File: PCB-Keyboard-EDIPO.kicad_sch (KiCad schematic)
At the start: 0 parts

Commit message: MCU Edits
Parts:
- added C1: 1u, symbol Device:C_Small
- added C2, C3: 22p, symbol Device:C_Small
- added C4, C5, C6, C7: 0.1u, symbol Device:C_Small
- added C8: 10u, symbol Device:C_Small
- added J1: AVR-ISP-6, symbol Connector:AVR-ISP-6
- added R1: 10k, symbol Device:R_Small
- added U1: ATmega32U4-A, Package_QFP:TQFP-44_10x10mm_P0.8mm, symbol MCU_Microchip_ATmega:ATmega32U4-A
- added Y1: XTAL, symbol Device:Crystal_GND24_Small
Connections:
- new net: R1.1, U1.33 (~{HWB}/PE2)
- new net: C1.1, U1.6 (UCAP)
- new net +5V: C4.1, C5.1, C6.1, C7.1, C8.1, J1.2 (VCC), U1.14 (VCC), U1.2 (UVCC), U1.24 (AVCC), U1.34 (VCC), U1.44 (AVCC)
- new net D+: U1.4 (D+)
- new net D-: U1.3 (D-)
- new net GND: C1.2, C2.2, C3.2, C4.2, C5.2, C6.2, C7.2, C8.2, J1.6 (GND), R1.2, U1.15 (GND), U1.23 (GND), U1.35 (GND), U1.43 (GND), U1.5 (UGND), Y1.2, Y1.4
- new net MISO: J1.1 (MISO), U1.11 (PB3)
- new net MOSI: J1.4 (MOSI), U1.10 (PB2)
- new net RESET: U1.13 (~{RESET})
- new net RST: J1.5 (~{RST})
- new net SCK: J1.3 (SCK), U1.9 (PB1)
- new net XTAL1: C3.1, U1.17 (XTAL1), Y1.1
- new net XTAL2: C2.1, U1.16 (XTAL2), Y1.3
- no-connect marks 0 -> 2

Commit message: Part 1
MCU, USB Port, Switch Matrix
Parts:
- added F1: 500m, symbol Device:Polyfuse_Small
- added R2: 10k, symbol Device:R_Small
- added R3, R4: 22, symbol Device:R_Small
- added R5, R6: 5.1k, symbol Device:R_Small
- added SW1: SW_Push_Reset, symbol local:SW_SKQG
- added U2: PRTR5V0U2X, symbol random-keyboard-parts:PRTR5V0U2X
- added USB1: HRO-TYPE-C-31-M-12, symbol Type-C:HRO-TYPE-C-31-M-12
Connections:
- net RST is gone; now on net RESET: J1.5 (~{RST})
- net +5V: now also U1.7 (VBUS), F1.2, R2.2
- net D+: now also R4.2
- net D-: now also R3.2
- net GND: now also R5.1, R6.1, SW1.2, U2.1 (GND), USB1.1 (GND), USB1.12 (GND), USB1.13 (SHIELD)
- new net: R5.2, USB1.10 (CC2)
- new net: R6.2, USB1.4 (CC1)
- new net DN: R3.1, U2.3 (IO2), USB1.5 (DN2), USB1.7 (DN1)
- new net DP: R4.1, U2.2 (IO1), USB1.6 (DP1), USB1.8 (DP2)
- new net Reset: R2.1, SW1.1
- new net VCC: F1.1, U2.4 (VCC), USB1.11 (VBUS), USB1.2 (VBUS)
- no-connect marks 2 -> 6
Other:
- moved on the sheet: C2, C3, J1, Y1

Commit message: Matrix Strart
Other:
- added sheet matrix (matrix.kicad_sch)
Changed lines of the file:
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@@
+		)
+	)
+	(sheet
+		(at 88.9 38.1)
+		(size 25.4 12.7)
+		(exclude_from_sim no)
+		(in_bom yes)
+		(on_board yes)
+		(dnp no)
+		(fields_autoplaced yes)
+		(stroke
+			(width 0.1524)
+			(type solid)
+		)
+		(fill
+			(color 0 0 0 0.0000)
+		)
+		(property "Sheetname" "matrix"
+			(at 88.9 37.3884 0)
+			(effects
+				(font
+					(size 1.27 1.27)
+				)
+				(justify left bottom)
+			)
+		)
+		(property "Sheetfile" "matrix.kicad_sch"
+			(at 88.9 51.3846 0)
+			(effects
+				(font
+					(size 1.27 1.27)
+				)
+				(justify left top)
+			)
+		)
+		(instances
+			(project "PCB-Keyboard-EDIPO"
+				(path "/8d1b740c-cc3b-4519-96ee-3a49fcc08051"
+					(page "2")
+				)
+			)
 		)
 	)

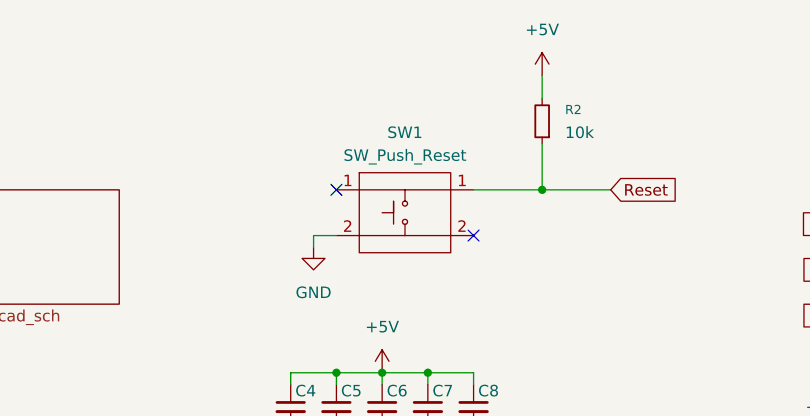
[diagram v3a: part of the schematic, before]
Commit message: Matrix Design and slight keycap config
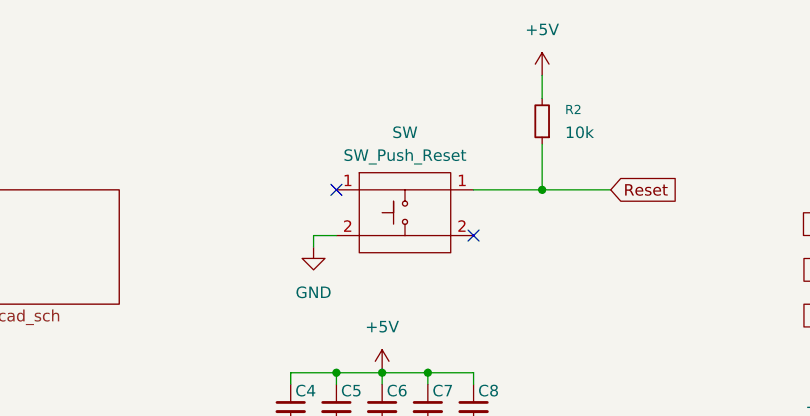
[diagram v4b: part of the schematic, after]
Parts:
- renumbered SW1 to SW
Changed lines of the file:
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@@
 		(dnp no)
 		(fields_autoplaced yes)
-		(property "Reference" "SW1"
+		(property "Reference" "SW"
 			(at 146.05 31.75 0)
 			(effects
@@
 			(project ""
 				(path "/8d1b740c-cc3b-4519-96ee-3a49fcc08051"
-					(reference "SW1")
+					(reference "SW")
 					(unit 1)
 				)

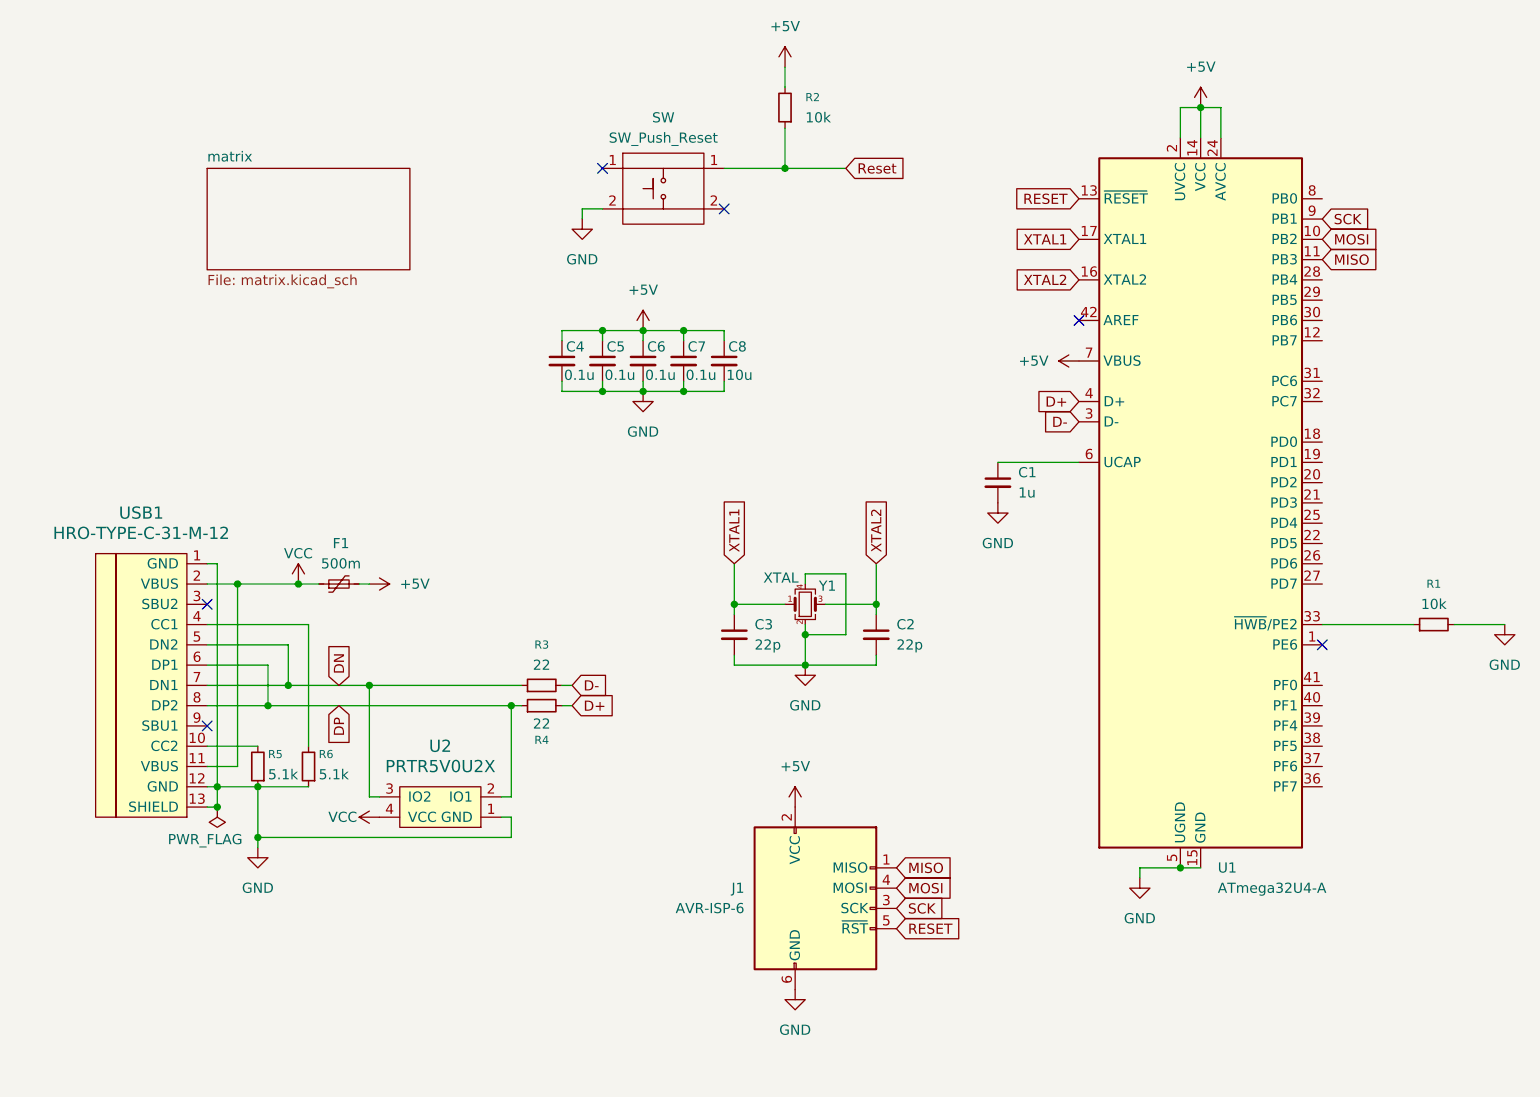
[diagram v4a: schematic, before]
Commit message: Matrix Design Done
still need to assign footprints
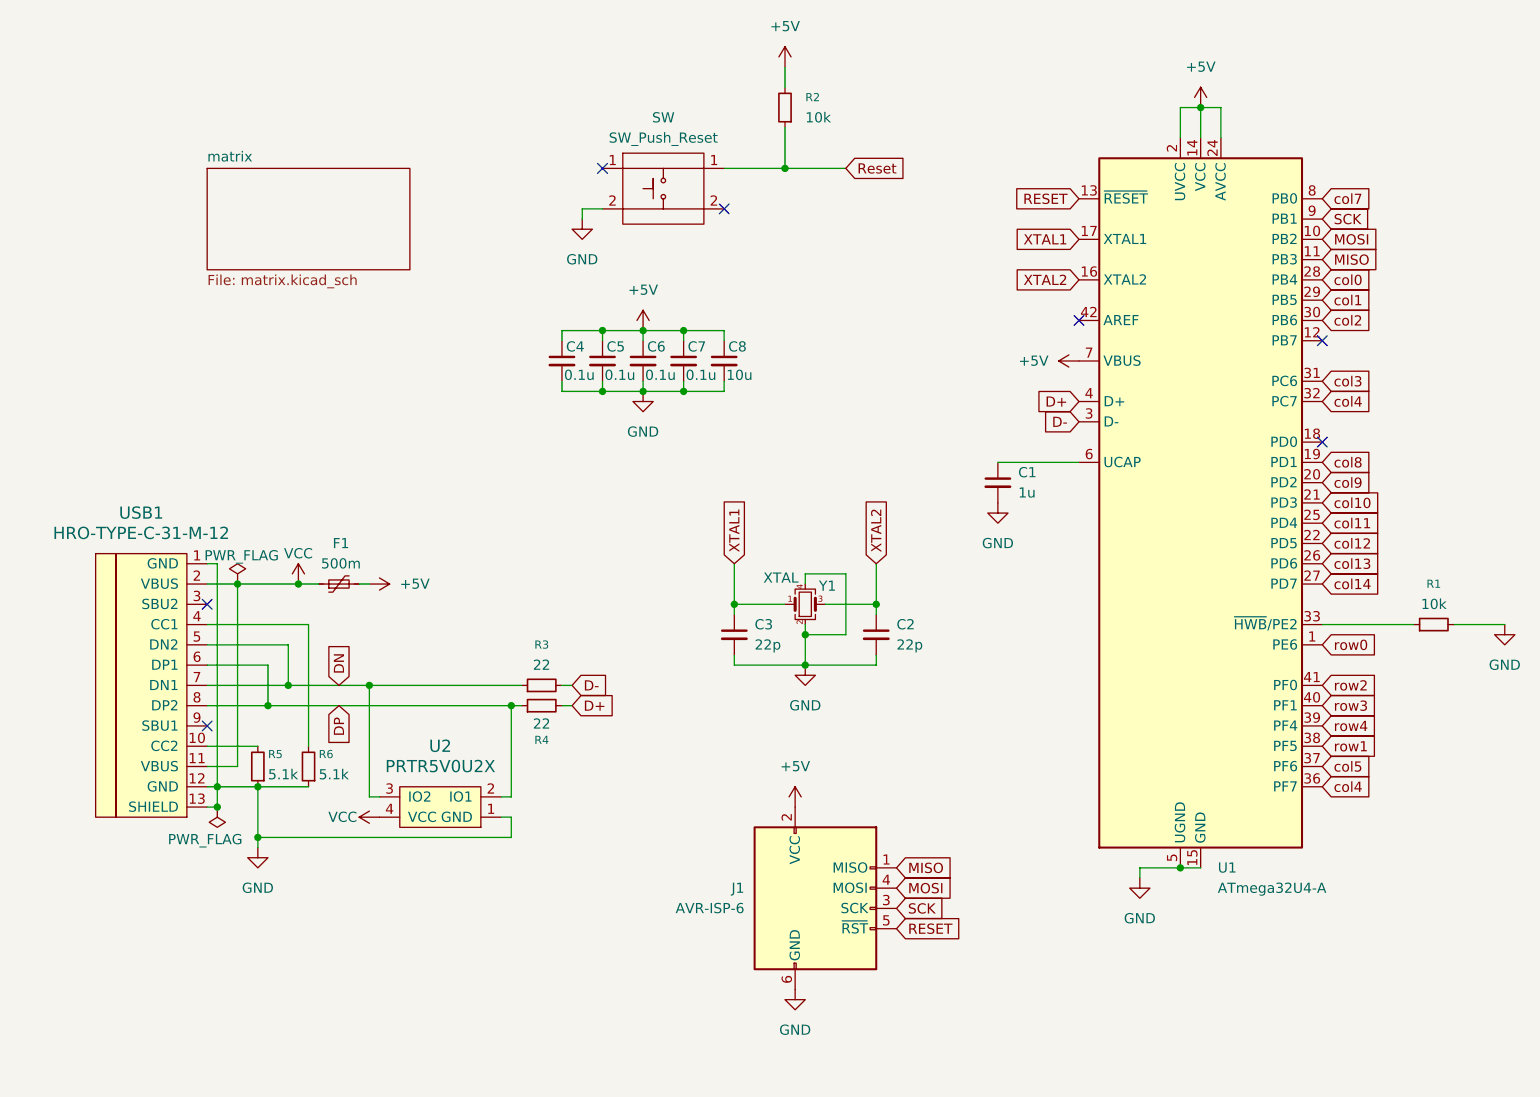
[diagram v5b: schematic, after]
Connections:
- net row0: now reaches U1.1 (PE6)
- net col8: now reaches U1.19 (PD1)
- net col9: now reaches U1.20 (PD2)
- net col10: now reaches U1.21 (PD3)
- net col12: now reaches U1.22 (PD5)
- net col11: now reaches U1.25 (PD4)
- net col13: now reaches U1.26 (PD6)
- net col14: now reaches U1.27 (PD7)
- net col0: now reaches U1.28 (PB4)
- net col1: now reaches U1.29 (PB5)
- net col2: now reaches U1.30 (PB6)
- net col3: now reaches U1.31 (PC6)
- net col4: now reaches U1.32 (PC7)
- net col4: now also U1.36 (PF7)
- net col5: now reaches U1.37 (PF6)
- net row1: now reaches U1.38 (PF5)
- net row4: now reaches U1.39 (PF4)
- net row3: now reaches U1.40 (PF1)
- net row2: now reaches U1.41 (PF0)
- net col7: now reaches U1.8 (PB0)
- no-connect marks 6 -> 7

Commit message: Footprints Added
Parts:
- C1, C2, C3, C4, C5, C6, C7, C8: footprint (none) -> Capacitor_SMD:C_0805_2012Metric_Pad1.18x1.45mm_HandSolder
- F1: footprint (none) -> Fuse:Fuse_1206_3216Metric_Pad1.42x1.75mm_HandSolder
- J1: footprint (none) -> random-keyboard-parts:Reset_Pretty-Mask
- R1, R2, R3, R4, R5, R6: footprint (none) -> Resistor_SMD:R_0805_2012Metric_Pad1.20x1.40mm_HandSolder
- SW68: renamed from SW; footprint (none) -> Button_Switch_SMD:SW_SPST_SKQG_WithStem
- U2: footprint (none) -> random-keyboard-parts:SOT143B
- USB1: footprint (none) -> Type-C:HRO-TYPE-C-31-M-12-HandSoldering
- Y1: footprint (none) -> Crystal:Crystal_SMD_3225-4Pin_3.2x2.5mm_HandSoldering
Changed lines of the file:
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@@
 			)
 		)
-		(property "Footprint" ""
+		(property "Footprint" "Capacitor_SMD:C_0805_2012Metric_Pad1.18x1.45mm_HandSolder"
 			(at 138.43 62.23 0)
 			(effects
@@
 			)
 		)
-		(property "Footprint" ""
+		(property "Footprint" "Capacitor_SMD:C_0805_2012Metric_Pad1.18x1.45mm_HandSolder"
 			(at 154.94 96.52 0)
 			(effects
@@
 			)
 		)
-		(property "Footprint" ""
+		(property "Footprint" "Resistor_SMD:R_0805_2012Metric_Pad1.20x1.40mm_HandSolder"
 			(at 130.81 102.87 0)
 			(effects
@@
 			)
 		)
-		(property "Footprint" ""
+		(property "Footprint" "Fuse:Fuse_1206_3216Metric_Pad1.42x1.75mm_HandSolder"
 			(at 110.49 88.9 0)
 			(effects
@@
 			)
 		)
-		(property "Footprint" ""
+		(property "Footprint" "Capacitor_SMD:C_0805_2012Metric_Pad1.18x1.45mm_HandSolder"
 			(at 172.72 96.52 0)
 			(effects
@@
 			)
 		)
-		(property "Footprint" ""
+		(property "Footprint" "Resistor_SMD:R_0805_2012Metric_Pad1.20x1.40mm_HandSolder"
 			(at 95.25 113.03 0)
 			(effects
@@
 			)
 		)
-		(property "Footprint" ""
+		(property "Footprint" "Resistor_SMD:R_0805_2012Metric_Pad1.20x1.40mm_HandSolder"
 			(at 161.29 30.48 0)
 			(effects
@@
 			)
 		)
-		(property "Footprint" ""
+		(property "Footprint" "random-keyboard-parts:Reset_Pretty-Mask"
 			(at 158.75 129.54 90)
 			(effects
@@
 			)
 		)
-		(property "Footprint" ""
+		(property "Footprint" "random-keyboard-parts:SOT143B"
 			(at 118.11 118.11 0)
 			(effects
@@
 			)
 		)
-		(property "Footprint" ""
+		(property "Footprint" "Capacitor_SMD:C_0805_2012Metric_Pad1.18x1.45mm_HandSolder"
 			(at 143.51 62.23 0)
 			(effects
@@
 			)
 		)
-		(property "Footprint" ""
+		(property "Footprint" "Type-C:HRO-TYPE-C-31-M-12-HandSoldering"
 			(at 86.36 101.6 0)
 			(effects
@@
 			)
 		)
-		(property "Footprint" ""
+		(property "Footprint" "Resistor_SMD:R_0805_2012Metric_Pad1.20x1.40mm_HandSolder"
 			(at 130.81 105.41 0)
 			(effects
@@
 			)
 		)
-		(property "Footprint" ""
+		(property "Footprint" "Resistor_SMD:R_0805_2012Metric_Pad1.20x1.40mm_HandSolder"
 			(at 101.6 113.03 0)
 			(effects
@@
 			)
 		)
-		(property "Footprint" ""
+		(property "Footprint" "Capacitor_SMD:C_0805_2012Metric_Pad1.18x1.45mm_HandSolder"
 			(at 148.59 62.23 0)
 			(effects
@@
 			)
 		)
-		(property "Footprint" ""
+		(property "Footprint" "Capacitor_SMD:C_0805_2012Metric_Pad1.18x1.45mm_HandSolder"
 			(at 153.67 62.23 0)
 			(effects
@@
 			)
 		)
-		(property "Footprint" ""
+		(property "Footprint" "Capacitor_SMD:C_0805_2012Metric_Pad1.18x1.45mm_HandSolder"
 			(at 187.96 77.47 0)
 			(effects
@@
 			)
 		)
-		(property "Footprint" ""
+		(property "Footprint" "Crystal:Crystal_SMD_3225-4Pin_3.2x2.5mm_HandSoldering"
 			(at 163.83 92.71 0)
 			(effects
@@
 		(dnp no)
 		(fields_autoplaced yes)
-		(property "Reference" "SW"
+		(property "Reference" "SW68"
 			(at 146.05 31.75 0)
 			(effects
@@
 			)
 		)
-		(property "Footprint" ""
+		(property "Footprint" "Button_Switch_SMD:SW_SPST_SKQG_WithStem"
 			(at 146.05 40.64 0)
 			(effects
@@
 			(project ""
 				(path "/8d1b740c-cc3b-4519-96ee-3a49fcc08051"
-					(reference "SW")
+					(reference "SW68")
 					(unit 1)
 				)
@@
 			)
 		)
-		(property "Footprint" ""
+		(property "Footprint" "Capacitor_SMD:C_0805_2012Metric_Pad1.18x1.45mm_HandSolder"
 			(at 133.35 62.23 0)
 			(effects
@@
 			)
 		)
-		(property "Footprint" ""
+		(property "Footprint" "Resistor_SMD:R_0805_2012Metric_Pad1.20x1.40mm_HandSolder"
 			(at 242.57 95.25 0)
 			(effects

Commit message: PCB Component Movement 1
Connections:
- net Reset is gone; now on net RESET: R2.1, SW68.1
- net +5V: now also F1.1; no longer F1.2
- net GND: now also R5.2, R6.2; no longer R5.1, R6.1
- net VCC: now also F1.2; no longer F1.1
- net at USB1.10 (CC2): now also R5.1; no longer R5.2
- net at USB1.4 (CC1): now also R6.1; no longer R6.2
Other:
- moved on the sheet: F1, R5, R6
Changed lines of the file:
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@@
 	)
 	(junction
+		(at 213.36 30.48)
+		(diameter 0)
+		(color 0 0 0 0)
+	)
+	(junction
 		(at 143.51 66.04)
 		(diameter 0)
@@
 		(color 0 0 0 0)
 	)
-	(junction
-		(at 213.36 30.48)
-		(diameter 0)
-		(color 0 0 0 0)
-	)
 	(no_connect
 		(at 88.9 92.71)
@@
 	(wire
 		(pts
+			(xy 215.9 34.29) (xy 215.9 30.48)
+		)
+		(stroke
+			(width 0)
+			(type default)
+		)
+	)
+	(wire
+		(pts
 			(xy 245.11 95.25) (xy 251.46 95.25)
 		)
@@
 	(wire
 		(pts
+			(xy 213.36 30.48) (xy 213.36 34.29)
+		)
+		(stroke
+			(width 0)
+			(type default)
+		)
+	)
+	(wire
+		(pts
 			(xy 96.52 100.33) (xy 96.52 105.41)
 		)
@@
 	(wire
 		(pts
+			(xy 213.36 25.4) (xy 213.36 30.48)
+		)
+		(stroke
+			(width 0)
+			(type default)
+		)
+	)
+	(wire
+		(pts
 			(xy 161.29 33.02) (xy 161.29 38.1)
 		)
@@
 	(wire
 		(pts
-			(xy 215.9 30.48) (xy 215.9 34.29)
+			(xy 133.35 105.41) (xy 134.62 105.41)
 		)
 		(stroke
@@
 	(wire
 		(pts
-			(xy 133.35 105.41) (xy 134.62 105.41)
+			(xy 138.43 58.42) (xy 138.43 59.69)
 		)
 		(stroke
@@
 	(wire
 		(pts
-			(xy 138.43 58.42) (xy 138.43 59.69)
+			(xy 95.25 115.57) (xy 95.25 121.92)
 		)
 		(stroke
@@
 	(wire
 		(pts
-			(xy 95.25 115.57) (xy 95.25 121.92)
+			(xy 210.82 34.29) (xy 210.82 30.48)
 		)
 		(stroke
@@
 	(wire
 		(pts
-			(xy 213.36 30.48) (xy 213.36 34.29)
-		)
-		(stroke
-			(width 0)
-			(type default)
-		)
-	)
-	(wire
-		(pts
 			(xy 163.83 96.52) (xy 163.83 100.33)
 		)
@@
 	(wire
 		(pts
-			(xy 210.82 30.48) (xy 213.36 30.48)
-		)
-		(stroke
-			(width 0)
-			(type default)
-		)
-	)
-	(wire
-		(pts
 			(xy 135.89 43.18) (xy 135.89 44.45)
 		)
@@
 	(wire
 		(pts
-			(xy 210.82 34.29) (xy 210.82 30.48)
+			(xy 88.9 102.87) (xy 99.06 102.87)
 		)
 		(stroke
@@
 	(wire
 		(pts
-			(xy 88.9 102.87) (xy 99.06 102.87)
+			(xy 133.35 64.77) (xy 133.35 66.04)
 		)
 		(stroke
@@
 	(wire
 		(pts
-			(xy 133.35 64.77) (xy 133.35 66.04)
+			(xy 172.72 100.33) (xy 172.72 99.06)
 		)
 		(stroke
@@
 	(wire
 		(pts
-			(xy 172.72 100.33) (xy 172.72 99.06)
+			(xy 148.59 58.42) (xy 153.67 58.42)
 		)
 		(stroke
@@
 	(wire
 		(pts
-			(xy 148.59 58.42) (xy 153.67 58.42)
+			(xy 168.91 96.52) (xy 168.91 88.9)
 		)
 		(stroke
@@
 	(wire
 		(pts
-			(xy 168.91 96.52) (xy 168.91 88.9)
+			(xy 138.43 64.77) (xy 138.43 66.04)
 		)
 		(stroke
@@
 	(wire
 		(pts
-			(xy 138.43 64.77) (xy 138.43 66.04)
+			(xy 210.82 30.48) (xy 213.36 30.48)
 		)
 		(stroke
@@
 	(wire
 		(pts
-			(xy 213.36 30.48) (xy 215.9 30.48)
+			(xy 154.94 99.06) (xy 154.94 100.33)
 		)
 		(stroke
@@
 	(wire
 		(pts
-			(xy 154.94 99.06) (xy 154.94 100.33)
+			(xy 215.9 30.48) (xy 213.36 30.48)
 		)
 		(stroke
@@
 		)
 	)
-	(global_label "Reset"
+	(global_label "RESET"
 		(shape input)
 		(at 168.91 38.1 0)
@@
 	(symbol
 		(lib_id "power:+5V")
-		(at 213.36 30.48 0)
+		(at 213.36 25.4 0)
 		(unit 1)
 		(exclude_from_sim no)
@@
 		(fields_autoplaced yes)
 		(property "Reference" "#PWR01"
-			(at 213.36 34.29 0)
+			(at 213.36 29.21 0)
 			(effects
 				(font
@@
 		)
 		(property "Value" "+5V"
-			(at 213.36 25.4 0)
+			(at 213.36 20.32 0)
 			(effects
 				(font
@@
 		)
 		(property "Footprint" ""
-			(at 213.36 30.48 0)
+			(at 213.36 25.4 0)
 			(effects
 				(font
@@
 		)
 		(property "Datasheet" ""
-			(at 213.36 30.48 0)
+			(at 213.36 25.4 0)
 			(effects
 				(font
@@
 		)
 		(property "Description" "Power symbol creates a global label with name \"+5V\""
-			(at 213.36 30.48 0)
+			(at 213.36 25.4 0)
 			(effects
 				(font
@@
 	(symbol
 		(lib_id "Device:Polyfuse_Small")
-		(at 105.41 90.17 90)
+		(at 105.41 90.17 270)
 		(unit 1)
 		(exclude_from_sim no)
@@
 		(dnp no)
 		(property "Reference" "F1"
-			(at 105.664 85.09 90)
+			(at 105.156 95.25 90)
 			(effects
 				(font
@@
 		)
 		(property "Value" "500m"
-			(at 105.664 87.63 90)
+			(at 105.156 92.71 90)
 			(effects
 				(font
@@
 		)
 		(property "Footprint" "Fuse:Fuse_1206_3216Metric_Pad1.42x1.75mm_HandSolder"
-			(at 110.49 88.9 0)
+			(at 100.33 91.44 0)
 			(effects
 				(font
@@
 	(symbol
 		(lib_id "Device:R_Small")
-		(at 95.25 113.03 180)
+		(at 95.25 113.03 0)
 		(unit 1)
 		(exclude_from_sim no)
@@
 		(dnp no)
 		(property "Reference" "R5"
-			(at 96.52 111.506 0)
+			(at 93.98 114.554 0)
 			(effects
 				(font
@@
 		)
 		(property "Value" "5.1k"
-			(at 96.52 114.046 0)
+			(at 93.98 112.014 0)
 			(effects
 				(font
@@
 	(symbol
 		(lib_id "Device:R_Small")
-		(at 101.6 113.03 180)
+		(at 101.6 113.03 0)
 		(unit 1)
 		(exclude_from_sim no)
@@
 		(dnp no)
 		(property "Reference" "R6"
-			(at 102.87 111.506 0)
+			(at 100.33 114.554 0)
 			(effects
 				(font
@@
 		)
 		(property "Value" "5.1k"
-			(at 102.87 114.046 0)
+			(at 100.33 112.014 0)
 			(effects
 				(font
